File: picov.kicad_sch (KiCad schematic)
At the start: 23 parts, among them J1 USB_C_Receptacle_USB2.0_16P, J2 Conn_01x20, J3 Conn_01x20, U1 RP2040, U2 AP2112K-3.3

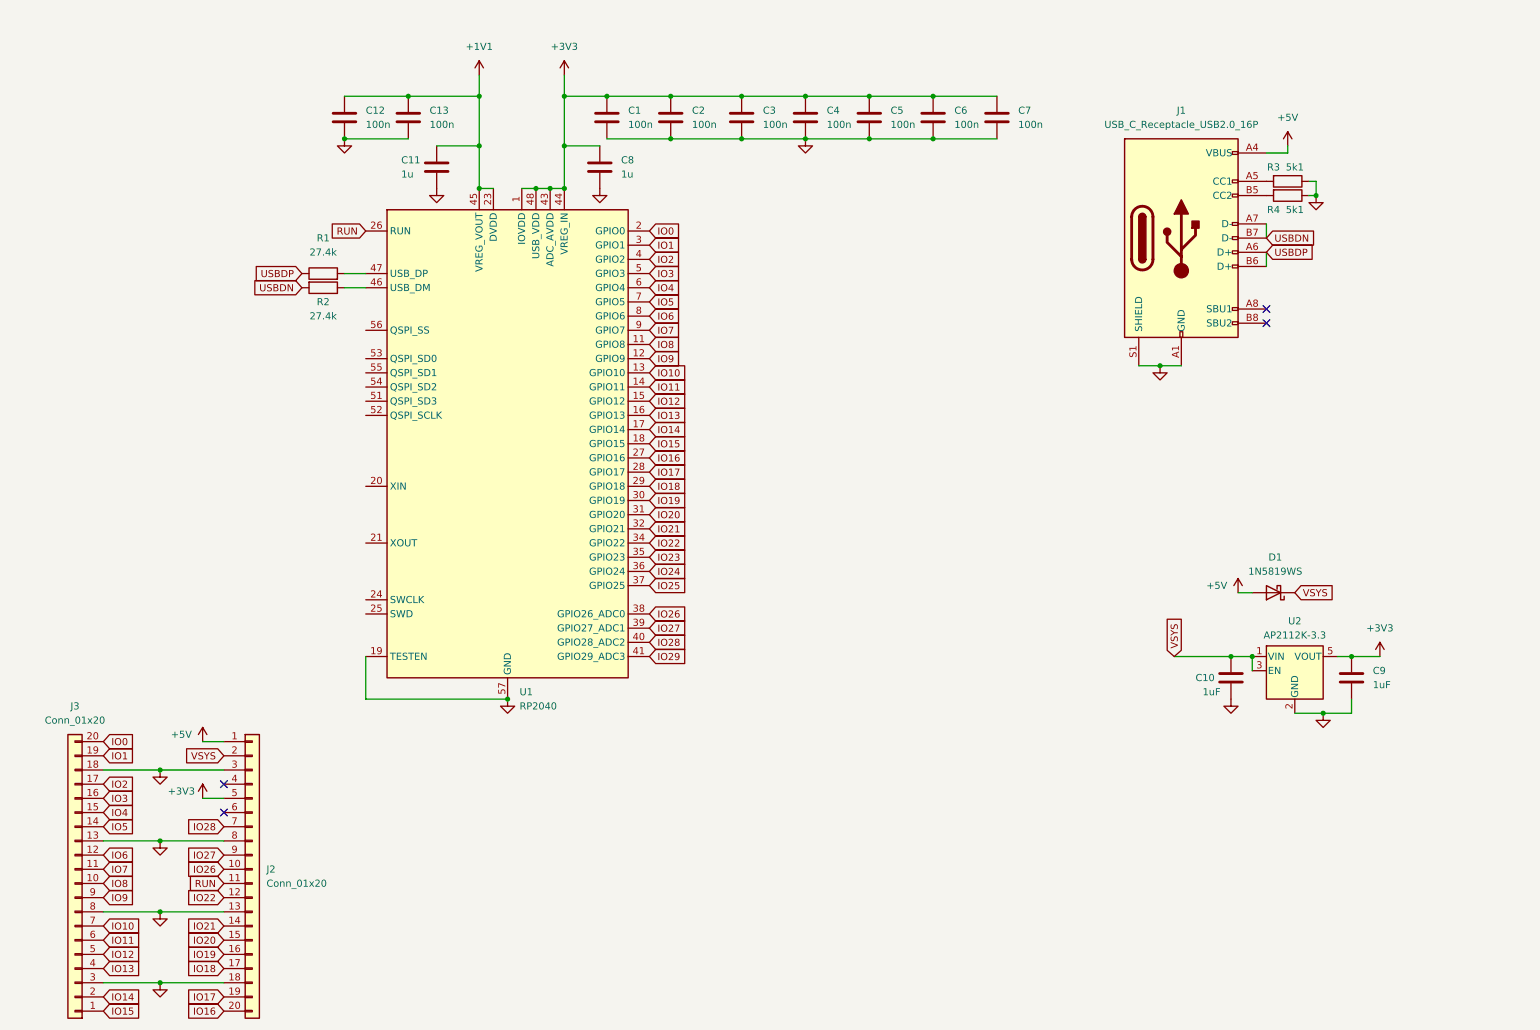
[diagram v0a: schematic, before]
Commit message: added castellated holes for sides, basic layout done
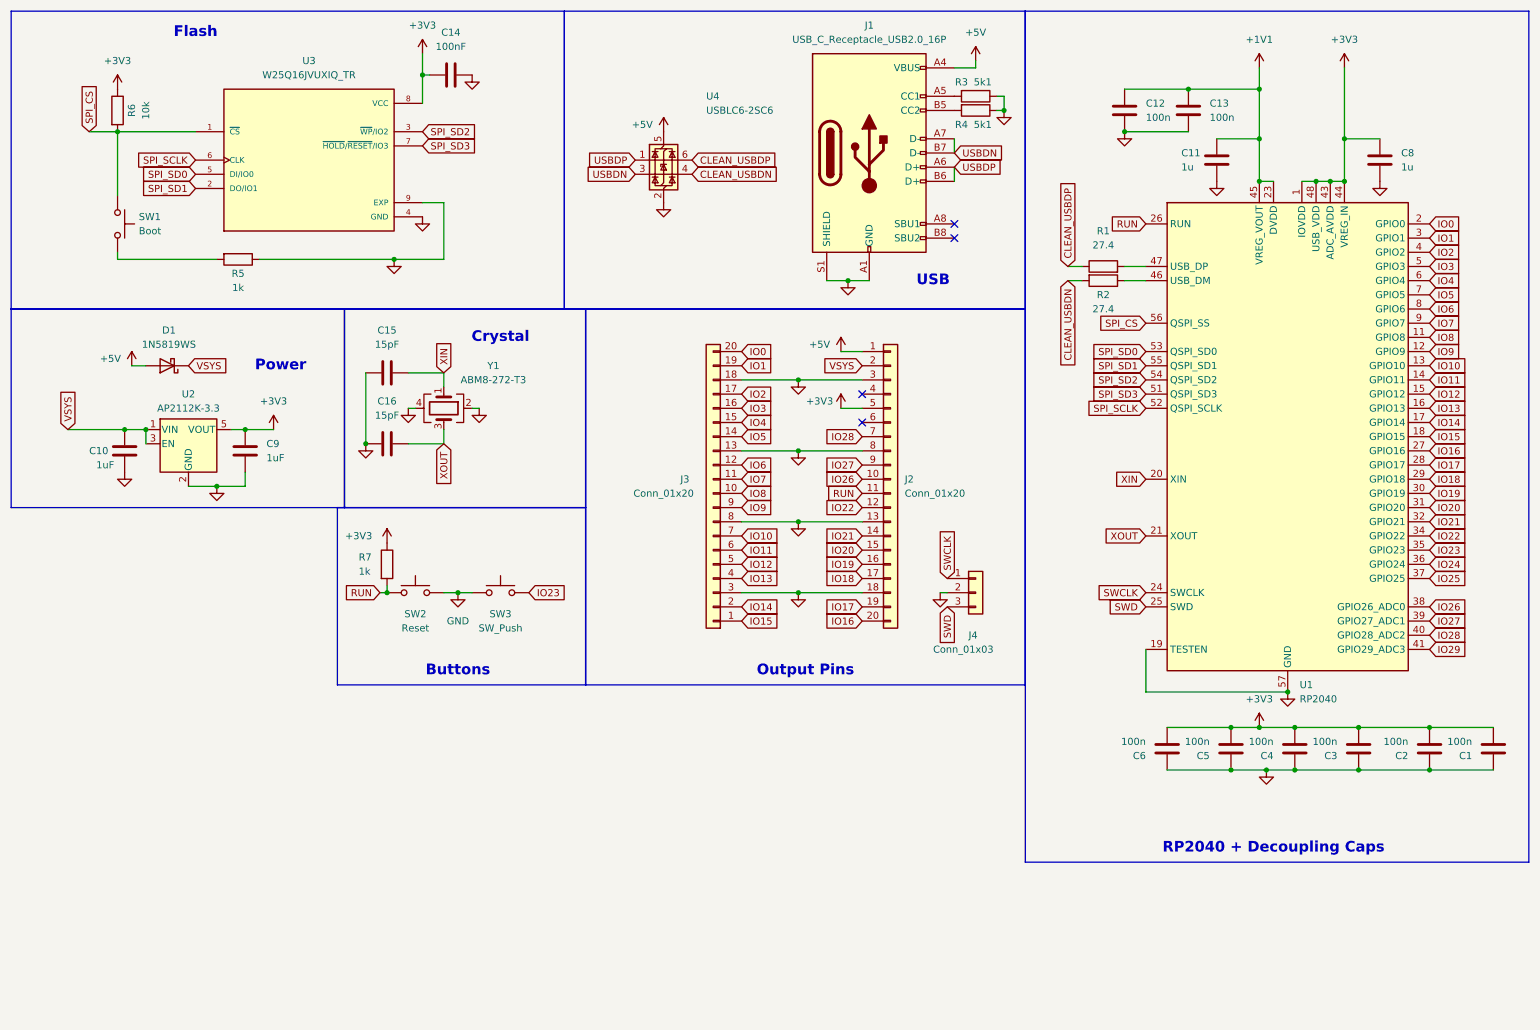
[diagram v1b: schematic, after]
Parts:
- removed C7: 100n, symbol Device:C
- added C14: 100nF, Capacitor_SMD:C_0402_1005Metric, symbol Device:C
- added C15, C16: 15pF, Capacitor_SMD:C_0402_1005Metric, symbol Device:C
- added J4: Conn_01x03, Connector_PinHeader_2.54mm:PinHeader_1x03_P2.54mm_Vertical, symbol Connector_Generic:Conn_01x03
- added R5, R7: 1k, Resistor_SMD:R_0402_1005Metric, symbol Device:R
- added R6: 10k, Resistor_SMD:R_0402_1005Metric, symbol Device:R
- added SW1: Boot, Button_Switch_SMD:SW_Push_SPST_NO_Alps_SKRK, symbol Switch:SW_Push
- added SW2: Reset, Button_Switch_SMD:SW_Push_SPST_NO_Alps_SKRK, symbol Switch:SW_Push
- added SW3: SW_Push, Button_Switch_SMD:SW_Push_SPST_NO_Alps_SKRK, symbol Switch:SW_Push
- added U3: W25Q16JVUXIQ_TR, W25Q16JVUXIQ_TR:IC_W25Q16JVUXIQ_TR, symbol W25Q16JVUXIQ_TR:W25Q16JVUXIQ_TR
- added U4: USBLC6-2SC6, Package_TO_SOT_SMD:SOT-23-6, symbol Power_Protection:USBLC6-2SC6
- added Y1: ABM8-272-T3, Crystal:Crystal_SMD_3225-4Pin_3.2x2.5mm, symbol Device:Crystal_GND24
- C1, C10, C11, C12, C13, C2, C3, C4, C5, C6, C8, C9: footprint (none) -> Capacitor_SMD:C_0402_1005Metric
- D1: footprint (none) -> Diode_SMD:D_SOD-123
- J1: footprint (none) -> Connector_USB:USB_C_Receptacle_G-Switch_GT-USB-7010ASV
- J2, J3: footprint (none) -> Connector_PinHeader_2.54mm:Castellated_20
- R1, R2: value 27.4k -> 27.4; footprint (none) -> Resistor_SMD:R_0402_1005Metric
- R3, R4: footprint Resistor_SMD:R_0805_2012Metric -> Resistor_SMD:R_0402_1005Metric
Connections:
- net +3V3: now also C1.2, C2.2, C3.2, C4.2, C5.2, C6.2, C14.1, R6.1, R7.1, U3.8 (VCC); no longer C1.1, C2.1, C3.1, C4.1, C5.1, C6.1
- net +5V: now also U4.5 (VBUS)
- net GND: now also C1.1, C2.1, C3.1, C4.1, C5.1, C6.1, C14.2, C15.1, C16.1, J4.2 (Pin_2), R5.1, SW2.2, SW3.1, U3.4 (GND), U3.9 (EXP), U4.2 (GND), Y1.2, Y1.4; no longer C1.2, C2.2, C3.2, C4.2, C5.2, C6.2
- net IO23: now also SW3.2
- net RUN: now also R7.2, SW2.1
- net USBDN: now also U4.3 (I/O2); no longer R2.2
- net USBDP: now also U4.1 (I/O1); no longer R1.1
- net XIN: now reaches U1.20 (XIN)
- net XIN: now also C15.2, Y1.1
- net XOUT: now reaches U1.21 (XOUT)
- net XOUT: now also C16.2, Y1.3
- net SWCLK: now reaches U1.24 (SWCLK)
- net SWCLK: now also J4.1 (Pin_1)
- net SWD: now reaches U1.25 (SWD)
- net SWD: now also J4.3 (Pin_3)
- net SPI_SD3: now reaches U1.51 (QSPI_SD3)
- net SPI_SD3: now also U3.7 (~{HOLD}/~{RESET}/IO3)
- net SPI_SCLK: now reaches U1.52 (QSPI_SCLK)
- net SPI_SCLK: now also U3.6 (CLK)
- net SPI_SD0: now reaches U1.53 (QSPI_SD0)
- net SPI_SD0: now also U3.5 (DI/IO0)
- net SPI_SD2: now reaches U1.54 (QSPI_SD2)
- net SPI_SD2: now also U3.3 (~{WP}/IO2)
- net SPI_SD1: now reaches U1.55 (QSPI_SD1)
- net SPI_SD1: now also U3.2 (DO/IO1)
- net SPI_CS: now reaches U1.56 (QSPI_SS)
- net SPI_CS: now also R6.2, SW1.1, U3.1 (~{CS})
- new net: R5.2, SW1.2
- new net CLEAN_USBDN: R2.2, U4.4 (I/O2)
- new net CLEAN_USBDP: R1.1, U4.6 (I/O1)
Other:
- note added: "Buttons"
- note added: "Crystal"
- note added: "Flash"
- note added: "Output Pins"
- note added: "Power"
- note added: "RP2040 + Decoupling Caps"
- note added: "USB"
- moved on the sheet: C1, C10, C11, C12, C13, C2, C3, C4, C5, C6, C8, C9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

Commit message: Finished all design for the pcb
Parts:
- C1, C12, C13, C2, C3, C4, C5, C6: value 100n -> 100nF; LCSC (none) -> C1525
- C10, C9: LCSC (none) -> C52923
- C11, C8: value 1u -> 1uF; LCSC (none) -> C52923
- C14: LCSC (none) -> C1525
- C15, C16: LCSC (none) -> C1548
- D1: LCSC (none) -> C191023
- J1: LCSC (none) -> C67380
- J2, J3, J4: now left out of the parts list
- R1, R2: value 27.4 -> 27; LCSC (none) -> C25100
- R3, R4: LCSC C27834 -> C25905
- R5, R7: LCSC (none) -> C11702
- R6: LCSC (none) -> C25744
- SW1: footprint Button_Switch_SMD:SW_Push_SPST_NO_Alps_SKRK -> Button_Switch_SMD:SW_Tactile_SPST_NO_Straight_CK_PTS636Sx25SMTRLFS; LCSC (none) -> C2858607
- SW2, SW3: footprint Button_Switch_SMD:SW_Push_SPST_NO_Alps_SKRK -> Button_Switch_SMD:SW_SPST_CK_KXT3; LCSC (none) -> C2858607
- U1: LCSC (none) -> C2040
- U2: LCSC (none) -> C51118
- U3: LCSC (none) -> C2843335
- U4: LCSC (none) -> C5180249
- Y1: LCSC (none) -> C9002
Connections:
- net +5V: no longer U4.5 (VBUS)
- net CLEAN_USBDN: now also U4.6 (I/O1); no longer U4.4 (I/O2)
- net CLEAN_USBDP: now also U4.4 (I/O2); no longer U4.6 (I/O1)
- net USBDN: now also U4.1 (I/O1); no longer U4.3 (I/O2)
- net USBDP: now also U4.3 (I/O2); no longer U4.1 (I/O1)
- net VSYS: now also U4.5 (VBUS)
- net FN: now reaches R2.1, U1.46 (USB_DM)
- net FP: now reaches R1.2, U1.47 (USB_DP)
